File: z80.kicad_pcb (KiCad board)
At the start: 2 copper layers, 5 parts, among them U1001 Z8400, U1002 AT28C64B, U1003 AS6C1008, U1004 Z8420, U1005 74LS138

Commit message: Commit before removing tracks
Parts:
- added P1: CONN_01X04, Pin_Headers:Pin_Header_Straight_1x04, F.Cu at (19.1, 95.2)
- added P2: CONN_02X20, Pin_Headers:Pin_Header_Angled_2x20, F.Cu at (95.2, 111.8)
- added P3: CONN_01X10, Pin_Headers:Pin_Header_Straight_1x10, F.Cu at (124.5, 25.4)
- added U1: 7400, Sockets_DIP:DIP-14__300_ELL, F.Cu at (64.8, 83.8)
- moved U1001 52.7 mm to (83.8, 50.8)
- moved U1002 22.2 mm to (31.8, 47.0)
- moved U1003 19.7 mm to (58.4, 47.0)
- moved U1004 7.85 mm to (108.0, 50.8)
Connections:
- U1001 pad 16: VCC -> /~INT
- U1001 pad 20: /~IOREQ -> /~IORQ
- U1003 pad 2: Net-(U1003-Pad2) -> GND
- U1003 pad 22: GND -> /~MREQ
- U1003 pad 24: /~MREQ -> /~RD
- U1004 pad 10: Net-(U1004-Pad10) -> /PIO_A4
- U1004 pad 12: Net-(U1004-Pad12) -> /PIO_A3
- U1004 pad 13: Net-(U1004-Pad13) -> /PIO_A2
- U1004 pad 14: Net-(U1004-Pad14) -> /PIO_A1
- U1004 pad 15: Net-(U1004-Pad15) -> /PIO_A0
- U1004 pad 16: VCC -> /~PIO_ASTB
- U1004 pad 18: Net-(U1004-Pad18) -> /PIO_ARDY
- U1004 pad 23: Net-(U1004-Pad23) -> /~INT
- U1004 pad 28: VCC -> Net-(U1004-Pad28)
- U1004 pad 37: /~M1 -> /~PIO_M1
- U1004 pad 7: Net-(U1004-Pad7) -> /PIO_A7
- U1004 pad 8: Net-(U1004-Pad8) -> /PIO_A6
- U1004 pad 9: Net-(U1004-Pad9) -> /PIO_A5
- U1005 pad 13: Net-(U1005-Pad13) -> /~CE_2
- U1005 pad 14: Net-(U1005-Pad14) -> /~CE_1
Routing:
- net /D5: track 26.2 -> 190.1 mm, vias 0 -> 3
- net /D4: track 67.6 -> 203.9 mm, vias 0 -> 3
- net /D7: track 26.2 -> 158.2 mm, vias 0 -> 1
- net /D6: track 26.2 -> 149.5 mm, vias 0 -> 2
- net /A3: track 35.1 -> 147.6 mm
- net /A2: track 35.1 -> 146.3 mm
- net /~RD: track 0.00 -> 108.1 mm, vias 0 -> 2
- net /A9: track 27.2 -> 134.5 mm, vias 0 -> 2
- net /A8: track 27.2 -> 133.9 mm, vias 0 -> 2
- net /D3: track 91.4 -> 196.3 mm, vias 0 -> 3
- net /A0: track 65.4 -> 157.7 mm, vias 0 -> 1
- net /A4: track 35.1 -> 118.1 mm
- net /~IORQ: track 0.00 -> 81.3 mm, vias 0 -> 1
- net /A5: track 35.1 -> 114.4 mm
- net /A6: track 35.1 -> 109.8 mm
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
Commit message: More routing
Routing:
- net /CLK: track 0.00 -> 228.0 mm, vias 0 -> 4
- net /~WR: track 0.00 -> 177.2 mm, vias 0 -> 5
- net /A12: track 61.9 -> 226.5 mm, vias 0 -> 2
- net /D2: track 131.7 -> 293.9 mm, vias 1 -> 6
- net /A15: track 23.4 -> 177.9 mm, vias 0 -> 4
- net /A14: track 27.3 -> 160.5 mm, vias 0 -> 1
- net /A10: track 28.8 -> 152.4 mm, vias 0 -> 3
- net /A11: track 57.6 -> 171.2 mm, vias 0 -> 3
- net /A13: track 19.5 -> 119.8 mm, vias 1 -> 3
- net /A8: track 133.9 -> 218.7 mm, vias 2 -> 4
- net /~IORQ: track 81.3 -> 0.00 mm, vias 1 -> 0
- net /PIO_A0: track 0.00 -> 59.5 mm
- net /A7: track 106.3 -> 165.6 mm, vias 1 -> 3
- net /A6: track 109.8 -> 165.2 mm, vias 0 -> 4
- net /A1: track 120.2 -> 175.2 mm, vias 1 -> 4
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
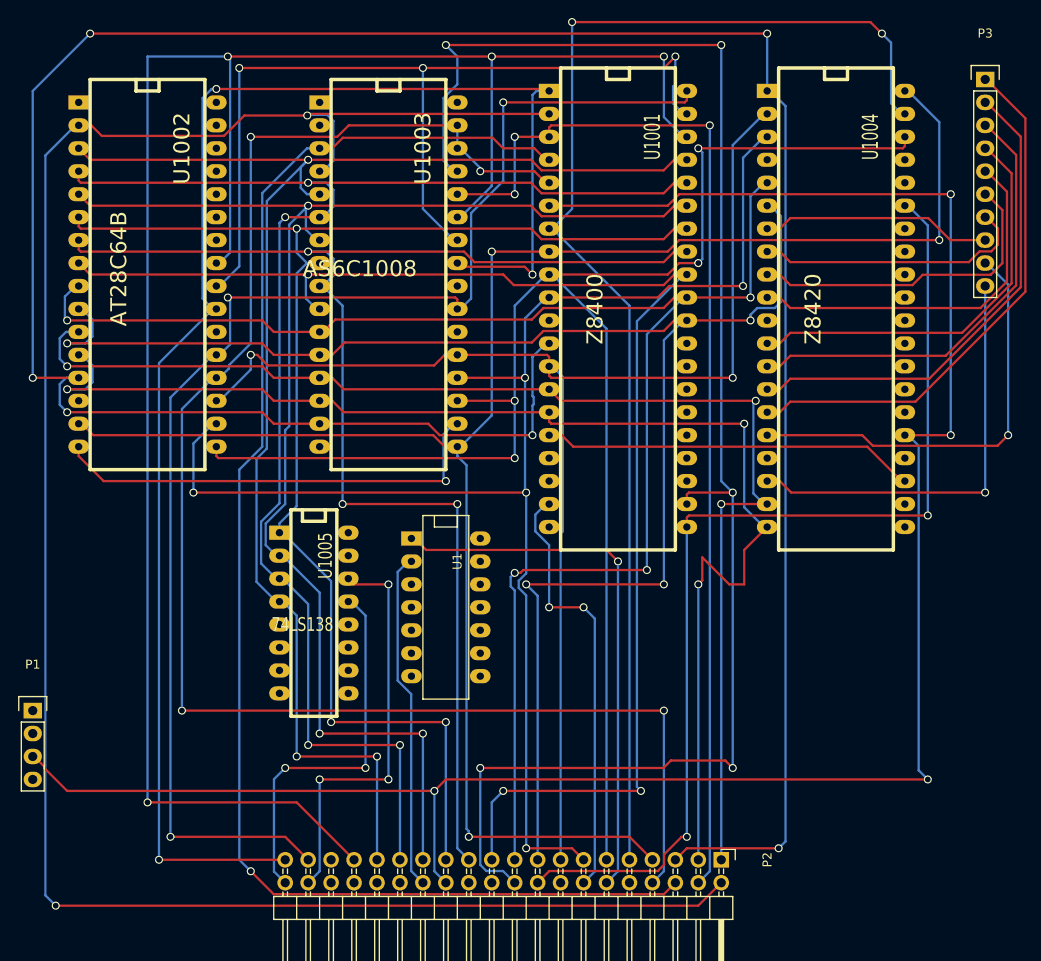
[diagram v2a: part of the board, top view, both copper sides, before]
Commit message: More routing. Adding decoupling and ~INT pull-up
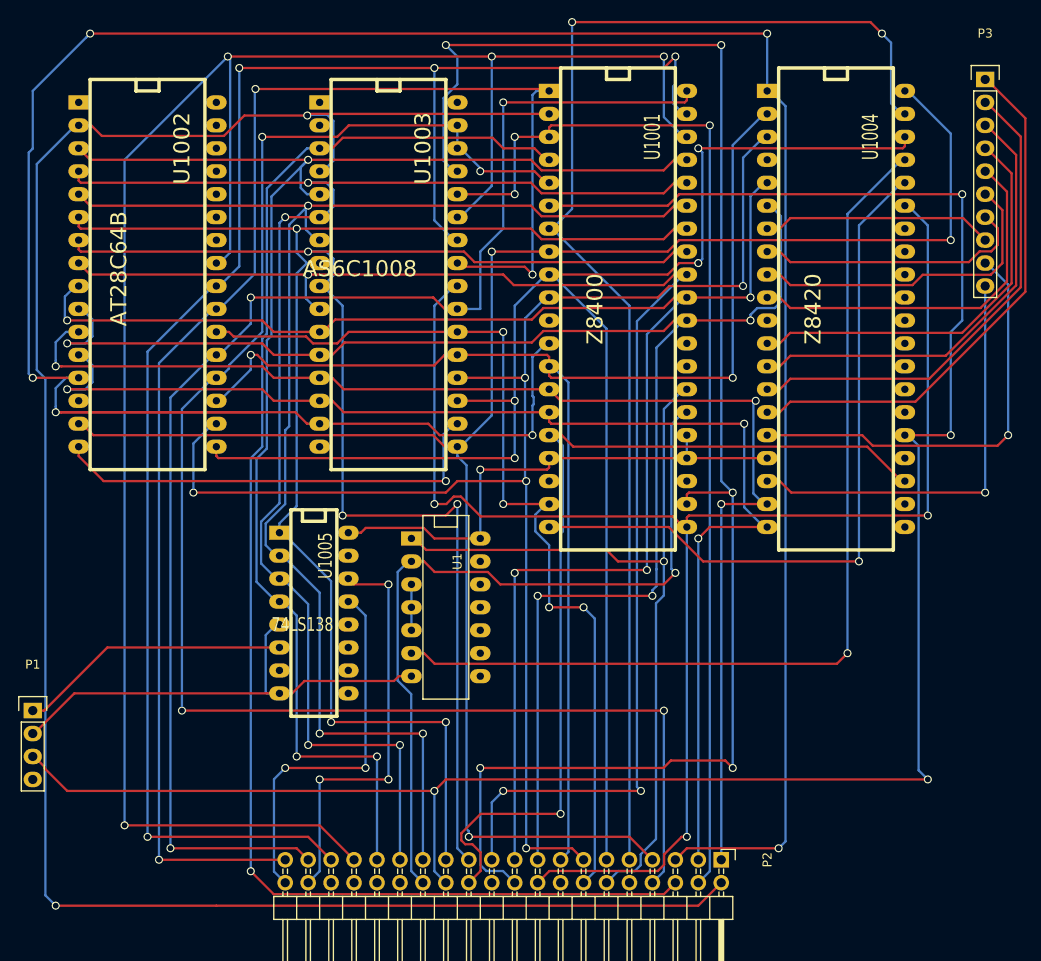
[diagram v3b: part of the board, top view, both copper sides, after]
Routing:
- net /~PIO_M1: track 0.00 -> 106.7 mm, vias 0 -> 1
- net VCC: track 0.00 -> 88.6 mm, vias 0 -> 1
- net /A9: track 102.3 -> 187.5 mm, vias 3 -> 4
- net /~IORQ: track 0.00 -> 80.1 mm, vias 0 -> 1
- net /~INT: track 41.5 -> 103.6 mm, vias 0 -> 1
- net /~MREQ: track 48.2 -> 105.2 mm, vias 2 -> 4
- net /~RD: track 116.9 -> 172.0 mm, vias 2 -> 3
- net GND: track 0.00 -> 54.4 mm
- net /~RESET: track 37.6 -> 87.2 mm, vias 0 -> 1
- net /~M1: track 60.0 -> 88.6 mm
- net /D2: track 293.9 -> 318.2 mm
- net Net-(U1-Pad3): track 0.00 -> 5.08 mm
- net /A11: track 171.2 -> 167.5 mm
- net /D1: track 143.7 -> 140.5 mm
- net /A0: track 177.5 -> 175.0 mm
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
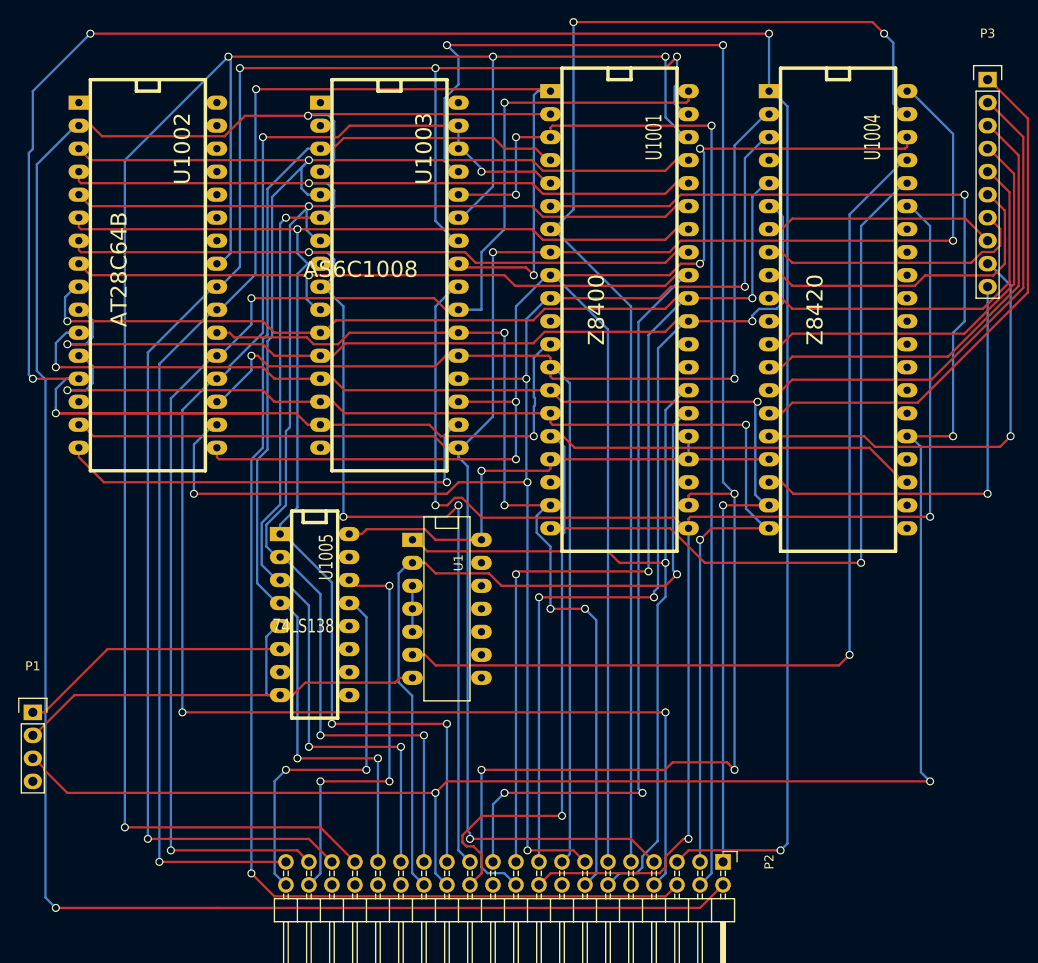
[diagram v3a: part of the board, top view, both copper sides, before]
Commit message: Add crystal clock circuit
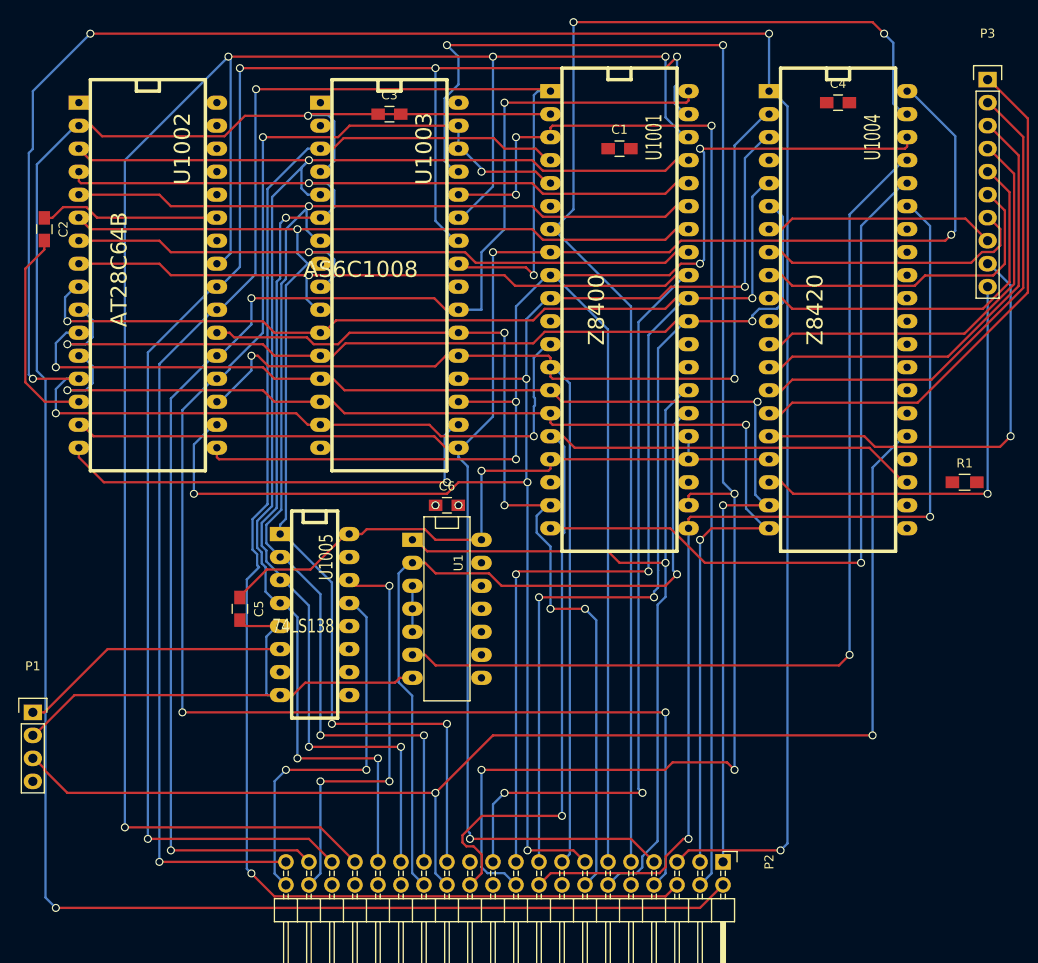
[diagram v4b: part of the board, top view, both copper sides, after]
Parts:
- added C1: 0.1u, Capacitors_SMD:C_0805_HandSoldering, F.Cu at (83.8, 33.0)
- added C2: 0.1u, Capacitors_SMD:C_0805_HandSoldering, F.Cu at (20.3, 41.9)
- added C3: 0.1u, Capacitors_SMD:C_0805_HandSoldering, F.Cu at (58.4, 29.2)
- added C4: 0.1u, Capacitors_SMD:C_0805_HandSoldering, F.Cu at (108.0, 27.9)
- added C5: 0.1u, Capacitors_SMD:C_0805_HandSoldering, F.Cu at (41.9, 83.8)
- added C6: 0.1u, Capacitors_SMD:C_0805_HandSoldering, F.Cu at (64.8, 72.4)
- added R1: 10k, Resistors_SMD:R_0805_HandSoldering, F.Cu at (121.9, 69.8)
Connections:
- U1004 pad 28: Net-(U1004-Pad28) -> VCC
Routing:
- net /CLK: track 229.8 -> 142.5 mm, vias 4 -> 2
- net /A3: track 155.8 -> 75.8 mm, vias 3 -> 1
- net /~RD: track 172.0 -> 117.6 mm, vias 3 -> 2
- net VCC: track 88.6 -> 123.6 mm, vias 1 -> 2
- net GND: track 54.4 -> 82.5 mm, vias 0 -> 1
- net /D2: track 318.2 -> 295.3 mm
- net /A14: track 159.4 -> 160.5 mm
- net /A4: track 157.7 -> 157.1 mm

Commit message: Started on pcb. WIP
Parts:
- removed C1, C2, C3, C4, C5, C6: 0.1u, Capacitors_SMD:C_0805_HandSoldering
- removed P1: CONN_01X04, Pin_Headers:Pin_Header_Straight_1x04
- removed P2: CONN_02X20, Pin_Headers:Pin_Header_Angled_2x20
- removed P3: CONN_01X10, Pin_Headers:Pin_Header_Straight_1x10
- removed R1: 10k, Resistors_SMD:R_0805_HandSoldering
- removed U1: 7400, Sockets_DIP:DIP-14__300_ELL
- removed U1001: Z8400, DIP-40__600_ELL
- removed U1002: AT28C64B, DIP-32__600_ELL
- removed U1003: AS6C1008, DIP-32__600_ELL
- removed U1004: Z8420, DIP-40__600_ELL
- removed U1005: 74LS138, DIP-16__300_ELL
- added 10k201: R, Resistor_SMD:R_0805_2012Metric_Pad1.20x1.40mm_HandSolder, F.Cu at (116.3, 55.3)
- added 10k202: R, Resistor_SMD:R_0805_2012Metric_Pad1.20x1.40mm_HandSolder, F.Cu at (116.3, 58.3)
- added 10k203: R, Resistor_SMD:R_0805_2012Metric_Pad1.20x1.40mm_HandSolder, F.Cu at (116.3, 61.2)
- added 10k204: R, Resistor_SMD:R_0805_2012Metric_Pad1.20x1.40mm_HandSolder, F.Cu at (116.3, 64.2)
- added 10k205: R, Resistor_SMD:R_0805_2012Metric_Pad1.20x1.40mm_HandSolder, F.Cu at (116.3, 67.1)
- added 10k206: R, Resistor_SMD:R_0805_2012Metric_Pad1.20x1.40mm_HandSolder, F.Cu at (116.3, 70.1)
- added 10k207: R, Resistor_SMD:R_0805_2012Metric_Pad1.20x1.40mm_HandSolder, F.Cu at (121.1, 55.3)
- added 10k208: R, Resistor_SMD:R_0805_2012Metric_Pad1.20x1.40mm_HandSolder, F.Cu at (121.1, 58.3)
- added 10k209: R, Resistor_SMD:R_0805_2012Metric_Pad1.20x1.40mm_HandSolder, F.Cu at (121.1, 61.2)
- added 10k210: R, Resistor_SMD:R_0805_2012Metric_Pad1.20x1.40mm_HandSolder, F.Cu at (121.1, 64.2)
- added 10k211: R, Resistor_SMD:R_0805_2012Metric_Pad1.20x1.40mm_HandSolder, F.Cu at (121.1, 67.1)
- added 10k212: R, Resistor_SMD:R_0805_2012Metric_Pad1.20x1.40mm_HandSolder, F.Cu at (121.1, 70.1)
- added 10k213: R, Resistor_SMD:R_0805_2012Metric_Pad1.20x1.40mm_HandSolder, F.Cu at (125.8, 55.3)
- added 10k214: R, Resistor_SMD:R_0805_2012Metric_Pad1.20x1.40mm_HandSolder, F.Cu at (125.8, 58.3)
- added 10k215: R, Resistor_SMD:R_0805_2012Metric_Pad1.20x1.40mm_HandSolder, F.Cu at (125.8, 61.2)
- added C101: 0.1u, Capacitor_SMD:C_0805_2012Metric_Pad1.18x1.45mm_HandSolder, F.Cu at (80.0, 210.8)
- added C102: 0.1u, Capacitor_SMD:C_0805_2012Metric_Pad1.18x1.45mm_HandSolder, B.Cu at (45.7, 193.0)
- added C103: 0.1u, Capacitor_SMD:C_0805_2012Metric_Pad1.18x1.45mm_HandSolder, B.Cu at (73.7, 185.4)
- added C104: 0.1u, Capacitor_SMD:C_0805_2012Metric_Pad1.18x1.45mm_HandSolder, B.Cu at (101.6, 170.2)
- added C105: 0.1u, Capacitor_SMD:C_0805_2012Metric_Pad1.18x1.45mm_HandSolder, F.Cu at (97.0, 210.8)
- added C106: 0.1u, Capacitor_SMD:C_0805_2012Metric_Pad1.18x1.45mm_HandSolder, F.Cu at (132.1, 205.7)
- added C107: 22pF, Capacitor_SMD:C_0805_2012Metric_Pad1.18x1.45mm_HandSolder, F.Cu at (80.6, 88.5)
- added C108: 22pF, Capacitor_SMD:C_0805_2012Metric_Pad1.18x1.45mm_HandSolder, F.Cu at (80.6, 91.5)
- added C109: 10u, Capacitor_THT:CP_Radial_D10.0mm_P5.00mm, F.Cu at (48.3, 226.1)
- added C201: 10u, Capacitor_THT:CP_Radial_D10.0mm_P5.00mm, F.Cu at (166.4, 40.9)
- added D101: LED, LED_SMD:LED_0805_2012Metric_Pad1.15x1.40mm_HandSolder, F.Cu at (39.1, 228.6)
- added J201: Conn_02x06_Row_Letter_First, Connector_PinHeader_2.54mm:PinHeader_2x06_P2.54mm_Vertical, F.Cu at (142.8, 18.9)
- added P101: CONN_01X04, Connector_PinHeader_2.54mm:PinHeader_1x06_P2.54mm_Vertical, F.Cu at (124.5, 228.6)
- added P102: CONN_02X20, Connector_PinHeader_2.54mm:PinHeader_2x20_P2.54mm_Horizontal, F.Cu at (38.1, 154.9)
- added P103: CONN_01X10, Connector_PinHeader_2.54mm:PinHeader_1x10_P2.54mm_Vertical, F.Cu at (149.9, 167.6)
- added P104: CONN_01X10, Connector_PinHeader_2.54mm:PinHeader_1x10_P2.54mm_Vertical, F.Cu at (149.9, 199.9)
- added P201: Interrupt Daisy Chain SIO, Connector_PinHeader_2.54mm:PinHeader_1x04_P2.54mm_Vertical, F.Cu at (130.5, 56.1)
- added P202: Interrupt Daisy Chain CTC, Connector_PinHeader_2.54mm:PinHeader_1x04_P2.54mm_Vertical, F.Cu at (135.1, 56.1)
- added P203: CONN_02X10, Connector_PinHeader_2.54mm:PinHeader_2x10_P2.54mm_Vertical, F.Cu at (135.6, 18.9)
- added P204: Outputs, Connector_PinHeader_2.54mm:PinHeader_1x03_P2.54mm_Vertical, F.Cu at (142.8, 36.2)
- added P205: Inputs, Connector_PinHeader_2.54mm:PinHeader_1x04_P2.54mm_Vertical, F.Cu at (139.7, 56.1)
- added R101: 10k, Resistor_SMD:R_0805_2012Metric_Pad1.20x1.40mm_HandSolder, F.Cu at (49.0, 70.5)
- added R102: 10k, Resistor_SMD:R_0805_2012Metric_Pad1.20x1.40mm_HandSolder, F.Cu at (49.0, 73.5)
- added R103: 10k, Resistor_SMD:R_0805_2012Metric_Pad1.20x1.40mm_HandSolder, F.Cu at (49.0, 76.4)
- added R104: 10k, Resistor_SMD:R_0805_2012Metric_Pad1.20x1.40mm_HandSolder, F.Cu at (49.0, 79.4)
- added R105: 1M, Resistor_SMD:R_0805_2012Metric_Pad1.20x1.40mm_HandSolder, F.Cu at (49.0, 82.3)
- added R106: 2k, Resistor_SMD:R_0805_2012Metric_Pad1.20x1.40mm_HandSolder, F.Cu at (49.0, 85.3)
- added R107: 0, Resistor_SMD:R_0805_2012Metric_Pad1.20x1.40mm_HandSolder, F.Cu at (49.0, 88.2)
- added R108: 470, Resistor_SMD:R_0805_2012Metric_Pad1.20x1.40mm_HandSolder, F.Cu at (39.1, 223.5)
- added R201: 10k, Resistor_SMD:R_0805_2012Metric_Pad1.20x1.40mm_HandSolder, F.Cu at (125.8, 64.2)
- added R202: 15k, Resistor_SMD:R_0805_2012Metric_Pad1.20x1.40mm_HandSolder, F.Cu at (125.8, 67.1)
- added U101: 7400, Package_DIP:DIP-14_W7.62mm_Socket_LongPads, F.Cu at (76.2, 215.9)
- added U102: Z8400, Package_DIP:DIP-40_W15.24mm_Socket_LongPads, F.Cu at (38.1, 167.6)
- added U103: AT28C64B, Package_DIP:DIP-28_W15.24mm_Socket_LongPads, F.Cu at (66.0, 167.6)
- added U104: AS6C1008, Package_DIP:DIP-32_W15.24mm_LongPads, F.Cu at (94.0, 167.6)
- added U105: 74LS138, Package_DIP:DIP-16_W7.62mm_Socket_LongPads, F.Cu at (93.5, 215.9)
- added U106: Z8420, Package_DIP:DIP-40_W15.24mm_LongPads, F.Cu at (121.9, 167.6)
- added U201: Z8430, Package_DIP:DIP-28_W15.24mm_Socket, F.Cu at (116.0, 18.7)
- added U202: Z8440, Package_DIP:DIP-40_W15.24mm_Socket_LongPads, F.Cu at (96.7, 18.7)
- added Y101: 4MHz, Crystal:Crystal_HC49-4H_Vertical, F.Cu at (66.7, 228.0)
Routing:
- net /D2: track 295.3 -> 0.00 mm, vias 6 -> 0
- net /A12: track 227.2 -> 0.00 mm, vias 2 -> 0
- net /A8: track 218.6 -> 0.00 mm, vias 4 -> 0
- net /D3: track 201.3 -> 0.00 mm, vias 3 -> 0
- net /D4: track 192.6 -> 0.00 mm, vias 3 -> 0
- net /A9: track 187.5 -> 0.00 mm, vias 4 -> 0
- net /D5: track 184.3 -> 0.00 mm, vias 4 -> 0
- net /~WR: track 177.2 -> 0.00 mm, vias 5 -> 0
- net /A15: track 177.1 -> 0.00 mm, vias 4 -> 0
- net /A0: track 175.0 -> 0.00 mm, vias 4 -> 0
- net /A1: track 174.9 -> 0.00 mm, vias 4 -> 0
- net /A11: track 167.5 -> 0.00 mm, vias 3 -> 0
- net /A7: track 165.6 -> 0.00 mm, vias 3 -> 0
- net /A6: track 165.0 -> 0.00 mm, vias 4 -> 0
- net /D6: track 162.7 -> 0.00 mm, vias 5 -> 0
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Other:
- net class Default removed

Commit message: Begun pcb routing. WIP
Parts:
- C101, C105, C106: moved to B.Cu
- moved C104 16.5 mm to (101.6, 186.7), turned to -90 degrees
- moved C101 9.92 mm to (87.6, 217.2), turned to -90 degrees
- turned C105 to 180 degrees
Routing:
- net GND: track 0.00 -> 380.4 mm, vias 0 -> 12
- net VCC: track 0.00 -> 363.3 mm, vias 0 -> 8
- net CLK: track 0.00 -> 191.8 mm, vias 0 -> 4
- net A13: track 0.00 -> 99.0 mm, vias 0 -> 4
- net D1: track 0.00 -> 83.8 mm, vias 0 -> 5
- net D0: track 0.00 -> 83.1 mm, vias 0 -> 6
- net D7: track 0.00 -> 62.8 mm, vias 0 -> 3
- net A11: track 0.00 -> 62.4 mm, vias 0 -> 1
- net A14: track 0.00 -> 62.2 mm, vias 0 -> 2
- net D3: track 0.00 -> 62.0 mm, vias 0 -> 2
- net D2: track 0.00 -> 61.9 mm, vias 0 -> 1
- net D4: track 0.00 -> 58.4 mm, vias 0 -> 4
- net A15: track 0.00 -> 55.5 mm, vias 0 -> 2
- net A6: track 13.8 -> 68.2 mm, vias 0 -> 4
- net D5: track 0.00 -> 52.6 mm, vias 0 -> 2
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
